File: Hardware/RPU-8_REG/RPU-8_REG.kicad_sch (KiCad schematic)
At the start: 30 parts, among them J1 DATA_BUS, J2 ADDR_BUS, J3 CTRL_BUS, J4 Conn_01x03_Female, J5 REG_CTRL, J6 REG_BITS, U1 74HC245, U2 74HC245, U3 74HC377, U4 74HC377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

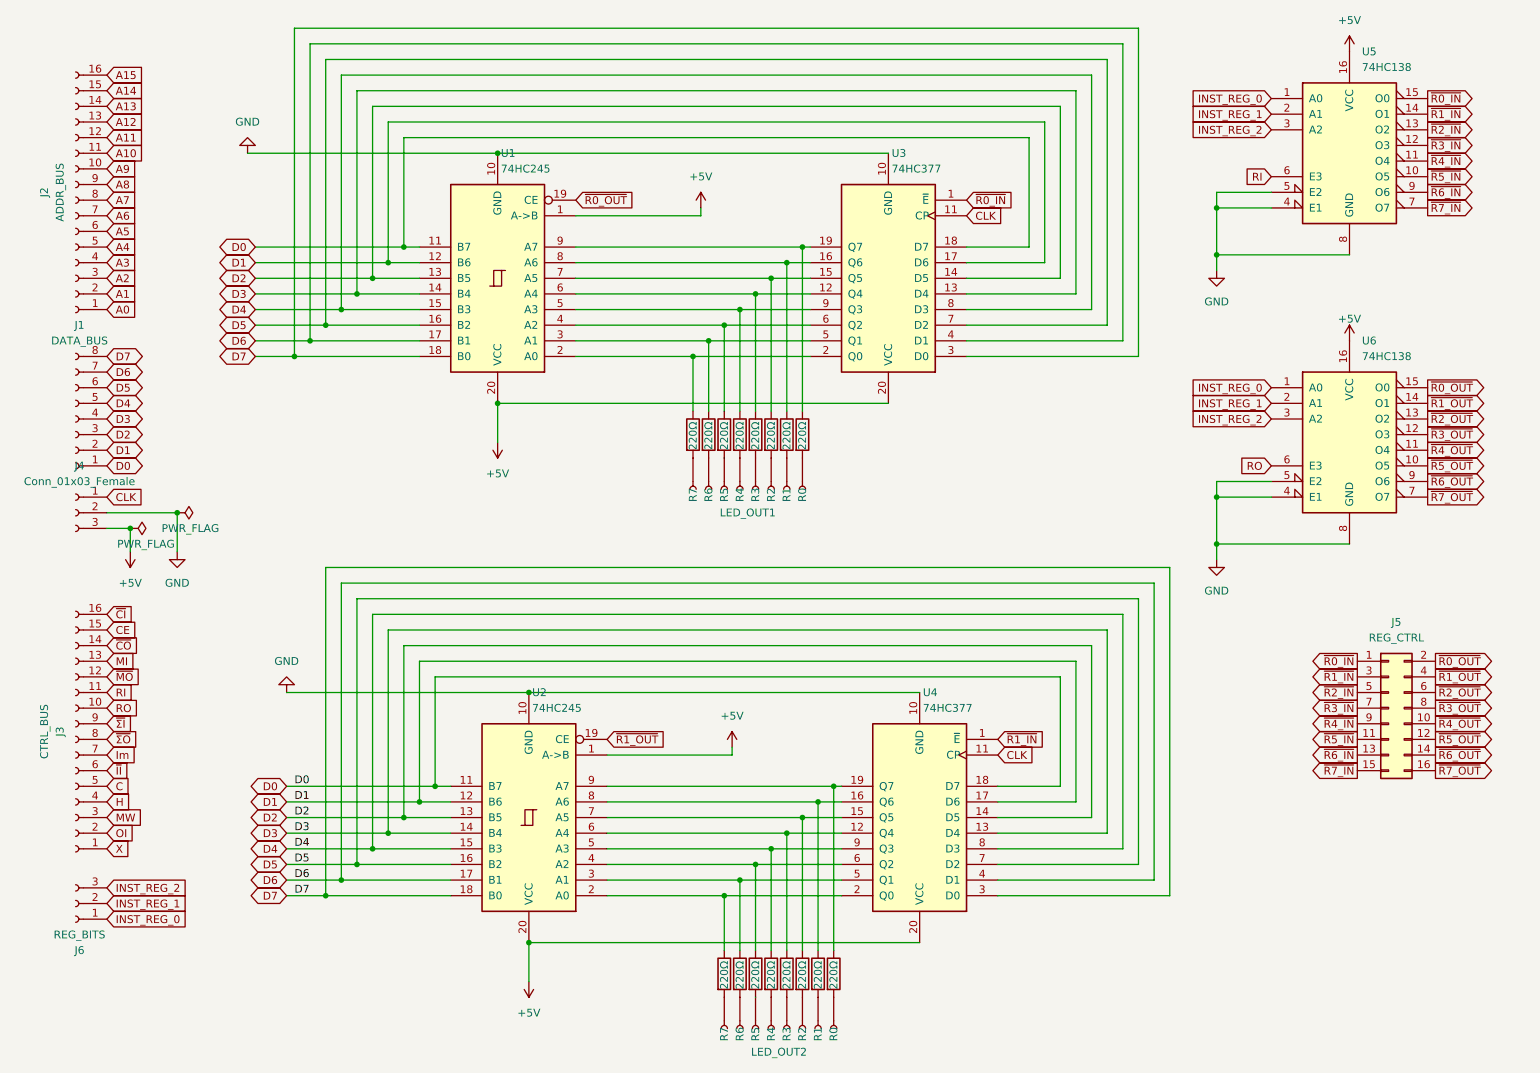
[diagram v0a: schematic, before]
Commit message: fixed REG layout
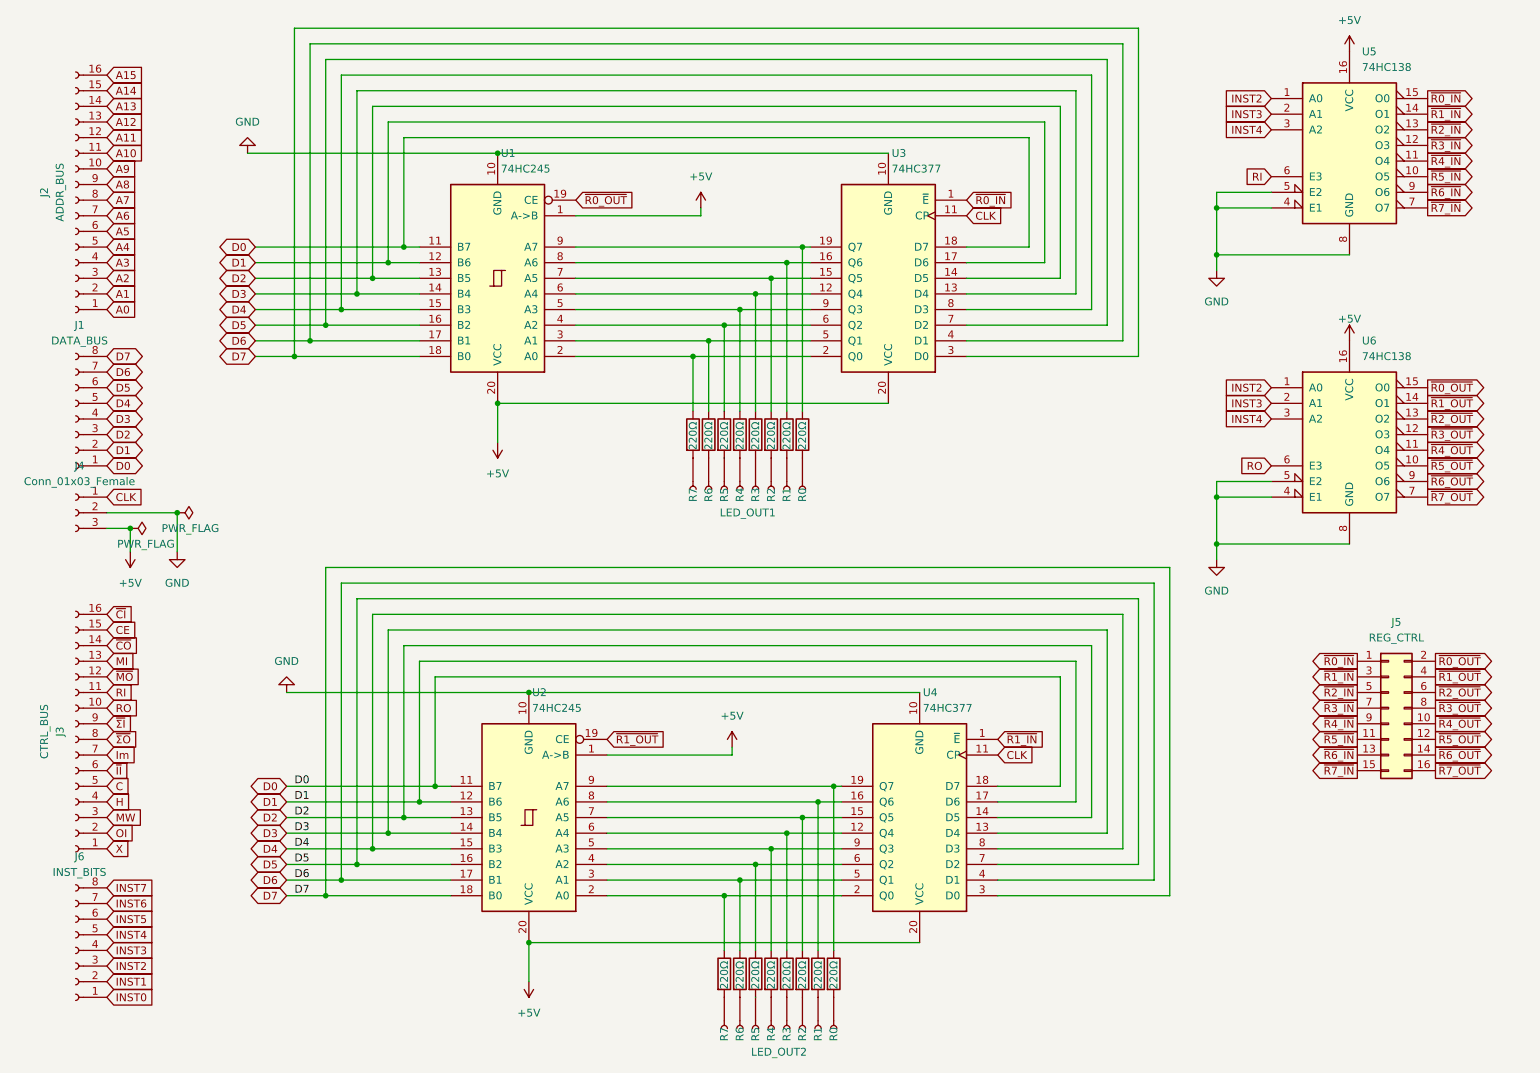
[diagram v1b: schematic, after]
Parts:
- J6: value REG_BITS -> INST_BITS; footprint Connector_PinSocket_2.54mm:PinSocket_1x04_P2.54mm_Vertical -> Connector_PinSocket_2.54mm:PinSocket_1x08_P2.54mm_Vertical; symbol Connector:Conn_01x03_Female -> Connector:Conn_01x08_Female
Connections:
- net INST_REG_0 renamed INST2
- net INST2: now also J6.3 (Pin_3); no longer J6.1 (Pin_1)
- net INST_REG_1 renamed INST3
- net INST3: now also J6.4 (Pin_4); no longer J6.2 (Pin_2)
- net INST_REG_2 renamed INST4
- net INST4: now also J6.5 (Pin_5); no longer J6.3 (Pin_3)
- new net INST0: J6.1 (Pin_1)
- new net INST1: J6.2 (Pin_2)
- new net INST5: J6.6 (Pin_6)
- new net INST6: J6.7 (Pin_7)
- new net INST7: J6.8 (Pin_8)
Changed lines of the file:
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@@
-    )
-  )
-  (global_label "INST_REG_1" (shape input) (at 222.25 30.48 180) (fields_autoplaced)
-    (effects (font (size 1.27 1.27)) (justify right))
-    (property "Intersheet References" "${INTERSHEET_REFS}" (id 0) (at 208.8907 30.4006 0)
-      (effects (font (size 1.27 1.27)) (justify right) hide)
     )
   )
@@
     )
   )
+  (global_label "INST4" (shape input) (at 222.25 33.02 180) (fields_autoplaced)
+    (effects (font (size 1.27 1.27)) (justify right))
+    (property "Intersheet References" "${INTERSHEET_REFS}" (id 0) (at 214.515 32.9406 0)
+      (effects (font (size 1.27 1.27)) (justify right) hide)
+    )
+  )
   (global_label "D2" (shape tri_state) (at 62.23 144.78 180) (fields_autoplaced)
     (effects (font (size 1.27 1.27)) (justify right))
@@
     )
   )
-  (global_label "INST_REG_2" (shape input) (at 222.25 33.02 180) (fields_autoplaced)
-    (effects (font (size 1.27 1.27)) (justify right))
-    (property "Intersheet References" "${INTERSHEET_REFS}" (id 0) (at 208.8907 32.9406 0)
-      (effects (font (size 1.27 1.27)) (justify right) hide)
-    )
-  )
   (global_label "D4" (shape tri_state) (at 57.15 62.23 180) (fields_autoplaced)
     (effects (font (size 1.27 1.27)) (justify right))
@@
     )
   )
+  (global_label "INST5" (shape input) (at 33.02 161.29 0) (fields_autoplaced)
+    (effects (font (size 1.27 1.27)) (justify left))
+    (property "Intersheet References" "${INTERSHEET_REFS}" (id 0) (at 40.755 161.2106 0)
+      (effects (font (size 1.27 1.27)) (justify left) hide)
+    )
+  )
   (global_label "~{R2_IN}" (shape output) (at 236.22 124.46 180) (fields_autoplaced)
     (effects (font (size 1.27 1.27)) (justify right))
@@
     )
   )
-  (global_label "INST_REG_0" (shape input) (at 222.25 27.94 180) (fields_autoplaced)
-    (effects (font (size 1.27 1.27)) (justify right))
-    (property "Intersheet References" "${INTERSHEET_REFS}" (id 0) (at 208.8907 27.8606 0)
-      (effects (font (size 1.27 1.27)) (justify right) hide)
-    )
-  )
-  (global_label "INST_REG_0" (shape input) (at 33.02 161.29 0) (fields_autoplaced)
-    (effects (font (size 1.27 1.27)) (justify left))
-    (property "Intersheet References" "${INTERSHEET_REFS}" (id 0) (at 46.3793 161.2106 0)
+  (global_label "INST0" (shape input) (at 33.02 173.99 0) (fields_autoplaced)
+    (effects (font (size 1.27 1.27)) (justify left))
+    (property "Intersheet References" "${INTERSHEET_REFS}" (id 0) (at 40.755 173.9106 0)
       (effects (font (size 1.27 1.27)) (justify left) hide)
     )
@@
     )
   )
-  (global_label "INST_REG_2" (shape input) (at 33.02 156.21 0) (fields_autoplaced)
-    (effects (font (size 1.27 1.27)) (justify left))
-    (property "Intersheet References" "${INTERSHEET_REFS}" (id 0) (at 46.3793 156.1306 0)
+  (global_label "INST2" (shape input) (at 222.25 27.94 180) (fields_autoplaced)
+    (effects (font (size 1.27 1.27)) (justify right))
+    (property "Intersheet References" "${INTERSHEET_REFS}" (id 0) (at 214.515 27.8606 0)
+      (effects (font (size 1.27 1.27)) (justify right) hide)
+    )
+  )
+  (global_label "INST2" (shape input) (at 33.02 168.91 0) (fields_autoplaced)
+    (effects (font (size 1.27 1.27)) (justify left))
+    (property "Intersheet References" "${INTERSHEET_REFS}" (id 0) (at 40.755 168.8306 0)
       (effects (font (size 1.27 1.27)) (justify left) hide)
     )
@@
     )
   )
+  (global_label "INST4" (shape input) (at 33.02 163.83 0) (fields_autoplaced)
+    (effects (font (size 1.27 1.27)) (justify left))
+    (property "Intersheet References" "${INTERSHEET_REFS}" (id 0) (at 40.755 163.7506 0)
+      (effects (font (size 1.27 1.27)) (justify left) hide)
+    )
+  )
+  (global_label "INST3" (shape input) (at 33.02 166.37 0) (fields_autoplaced)
+    (effects (font (size 1.27 1.27)) (justify left))
+    (property "Intersheet References" "${INTERSHEET_REFS}" (id 0) (at 40.755 166.2906 0)
+      (effects (font (size 1.27 1.27)) (justify left) hide)
+    )
+  )
   (global_label "D4" (shape tri_state) (at 62.23 149.86 180) (fields_autoplaced)
     (effects (font (size 1.27 1.27)) (justify right))
@@
     )
   )
-  (global_label "INST_REG_0" (shape input) (at 222.25 74.93 180) (fields_autoplaced)
-    (effects (font (size 1.27 1.27)) (justify right))
-    (property "Intersheet References" "${INTERSHEET_REFS}" (id 0) (at 208.8907 74.8506 0)
+  (global_label "INST2" (shape input) (at 222.25 74.93 180) (fields_autoplaced)
+    (effects (font (size 1.27 1.27)) (justify right))
+    (property "Intersheet References" "${INTERSHEET_REFS}" (id 0) (at 214.515 74.8506 0)
       (effects (font (size 1.27 1.27)) (justify right) hide)
     )
@@
     )
   )
-  (global_label "INST_REG_2" (shape input) (at 222.25 80.01 180) (fields_autoplaced)
-    (effects (font (size 1.27 1.27)) (justify right))
-    (property "Intersheet References" "${INTERSHEET_REFS}" (id 0) (at 208.8907 79.9306 0)
+  (global_label "INST4" (shape input) (at 222.25 80.01 180) (fields_autoplaced)
+    (effects (font (size 1.27 1.27)) (justify right))
+    (property "Intersheet References" "${INTERSHEET_REFS}" (id 0) (at 214.515 79.9306 0)
       (effects (font (size 1.27 1.27)) (justify right) hide)
     )
@@
     )
   )
+  (global_label "INST3" (shape input) (at 222.25 30.48 180) (fields_autoplaced)
+    (effects (font (size 1.27 1.27)) (justify right))
+    (property "Intersheet References" "${INTERSHEET_REFS}" (id 0) (at 214.515 30.4006 0)
+      (effects (font (size 1.27 1.27)) (justify right) hide)
+    )
+  )
   (global_label "~{R5_OUT}" (shape output) (at 248.92 132.08 0) (fields_autoplaced)
     (effects (font (size 1.27 1.27)) (justify left))
@@
     )
   )
+  (global_label "INST7" (shape input) (at 33.02 156.21 0) (fields_autoplaced)
+    (effects (font (size 1.27 1.27)) (justify left))
+    (property "Intersheet References" "${INTERSHEET_REFS}" (id 0) (at 40.755 156.1306 0)
+      (effects (font (size 1.27 1.27)) (justify left) hide)
+    )
+  )
   (global_label "RO" (shape input) (at 33.02 127 0) (fields_autoplaced)
     (effects (font (size 1.27 1.27)) (justify left))
@@
     )
   )
+  (global_label "INST6" (shape input) (at 33.02 158.75 0) (fields_autoplaced)
+    (effects (font (size 1.27 1.27)) (justify left))
+    (property "Intersheet References" "${INTERSHEET_REFS}" (id 0) (at 40.755 158.6706 0)
+      (effects (font (size 1.27 1.27)) (justify left) hide)
+    )
+  )
   (global_label "~{R6_IN}" (shape output) (at 247.65 43.18 0) (fields_autoplaced)
     (effects (font (size 1.27 1.27)) (justify left))
@@
     )
   )
-  (global_label "INST_REG_1" (shape input) (at 33.02 158.75 0) (fields_autoplaced)
-    (effects (font (size 1.27 1.27)) (justify left))
-    (property "Intersheet References" "${INTERSHEET_REFS}" (id 0) (at 46.3793 158.6706 0)
-      (effects (font (size 1.27 1.27)) (justify left) hide)
-    )
-  )
-  (global_label "INST_REG_1" (shape input) (at 222.25 77.47 180) (fields_autoplaced)
-    (effects (font (size 1.27 1.27)) (justify right))
-    (property "Intersheet References" "${INTERSHEET_REFS}" (id 0) (at 208.8907 77.3906 0)
+  (global_label "INST1" (shape input) (at 33.02 171.45 0) (fields_autoplaced)
+    (effects (font (size 1.27 1.27)) (justify left))
+    (property "Intersheet References" "${INTERSHEET_REFS}" (id 0) (at 40.755 171.3706 0)
+      (effects (font (size 1.27 1.27)) (justify left) hide)
+    )
+  )
+  (global_label "INST3" (shape input) (at 222.25 77.47 180) (fields_autoplaced)
+    (effects (font (size 1.27 1.27)) (justify right))
+    (property "Intersheet References" "${INTERSHEET_REFS}" (id 0) (at 214.515 77.3906 0)
       (effects (font (size 1.27 1.27)) (justify right) hide)
     )
@@
     (pin "2")
   )
-  (symbol (lib_id "Connector:Conn_01x03_Female") (at 27.94 158.75 180) (unit 1)
-    (in_bom yes) (on_board yes) (fields_autoplaced)
-    (property "Reference" "J6" (id 0) (at 28.575 166.37 0))
-    (property "Value" "REG_BITS" (id 1) (at 28.575 163.83 0))
-    (property "Footprint" "Connector_PinSocket_2.54mm:PinSocket_1x04_P2.54mm_Vertical" (id 2) (at 27.94 158.75 0)
-      (effects (font (size 1.27 1.27)) hide)
-    )
-    (property "Datasheet" "~" (id 3) (at 27.94 158.75 0)
+  (symbol (lib_id "Connector:Conn_01x08_Female") (at 27.94 166.37 180) (unit 1)
+    (in_bom yes) (on_board yes) (fields_autoplaced)
+    (property "Reference" "J6" (id 0) (at 28.575 151.13 0))
+    (property "Value" "INST_BITS" (id 1) (at 28.575 153.67 0))
+    (property "Footprint" "Connector_PinSocket_2.54mm:PinSocket_1x08_P2.54mm_Vertical" (id 2) (at 27.94 166.37 0)
+      (effects (font (size 1.27 1.27)) hide)
+    )
+    (property "Datasheet" "~" (id 3) (at 27.94 166.37 0)
       (effects (font (size 1.27 1.27)) hide)
     )
@@
     (pin "2")
     (pin "3")
+    (pin "4")
+    (pin "5")
+    (pin "6")
+    (pin "7")
+    (pin "8")
   )
   (symbol (lib_id "Device:R") (at 140.97 170.18 0) (unit 1)
@@
     )
     (path "/9c9f2ee9-43d0-47ee-b85b-95065a4ef97f"
-      (reference "J6") (unit 1) (value "REG_BITS") (footprint "Connector_PinSocket_2.54mm:PinSocket_1x04_P2.54mm_Vertical")
+      (reference "J6") (unit 1) (value "INST_BITS") (footprint "Connector_PinSocket_2.54mm:PinSocket_1x08_P2.54mm_Vertical")
     )
     (path "/e58d9857-6400-46b6-a3e7-f6906aabe732"
